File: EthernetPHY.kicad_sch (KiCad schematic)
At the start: 33 parts, among them IC2 DP83826IRHBR, J3 RJMG1S8008101BR, SW2 RESET, Y2 25MHz

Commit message: update
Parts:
- C11, C18: footprint Capacitor_SMD:C_0805_2012Metric -> Capacitor_SMD:C_0402_1005Metric; MPN (none) -> GRM155R71E103KA01D; Manufacturer (none) -> Murata Electronics
- C23: footprint Capacitor_SMD:C_0805_2012Metric -> Capacitor_SMD:C_0603_1608Metric
- D3, D4: footprint (none) -> LED_SMD:LED_0805_2012Metric
- SW2: value RESET -> SW_Push
- renumbered IC2 to U7
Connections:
- net +3.3V: now also C18.1; no longer C18.2
- net GND: now also C11.2, C18.2; no longer C11.1, C18.1
- net at C12.1, C13.1, C17.1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: now also C11.1; no longer C11.2
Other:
- note added: "PHY_RST"

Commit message: Done ERC + Documentation
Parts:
- added R36, R37, R42: 10k, Resistor_SMD:R_0603_1608Metric, symbol Device:R_US
- D8: renamed from D5; footprint ESD8104MUTAG -> footprints:ESD8104MUTAG; MPN (none) -> ESD7104MUTAG; Manufacturer_Part_Number ESD7104MUTAG -> (none)
- J6: renamed from J3; footprint RJMG1S8008101BR:AMPHENOL_RJMG1S8008101BR -> footprints:AMPHENOL_RJMG1S8008101BR; MPN (none) -> RJMG1S8008101BR
- renumbered C23 to C31, C22 to C32, C11 to C33, C12 to C34, C13 to C35, C15 to C36, C16 to C37, C14 to C38, C17 to C39, C18 to C40, C19 to C41, C20 to C42, C21 to C43, D4 to D10, D3 to D9, FB1 to FB2, R22 to R28, R16 to R29, R11 to R30, R13 to R31, R12 to R32, R14 to R33, R15 to R34, R18 to R35, R19 to R38, R23 to R39, R20 to R40, R21 to R41, SW2 to SW6, U7 to U5
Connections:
- net GND: now also R36.2, R37.2, R42.2
- net LED0: now also U5.30 (LED0/STRAP2)
- net at U5.22 (TX_CLK/STRAP5): now also R42.1
- net at U5.28 (COL/LED2/GPIO/STRAP4): now also R36.1
- net at U5.29 (CRS/LED3/STRAP3): now also R37.1
- no-connect marks 12 -> 9
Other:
- note added: "PHY Bootstrap table"
- moved on the sheet: C31, C32, C33, C34, C35, C36, C37, C38, C39, C40, C41, C42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

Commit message: Initial Review Changes
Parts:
- added TP5: RMII_REF_CLK, TestPoint:TestPoint_Pad_D1.0mm, symbol Connector:TestPoint
- J6: value RJMG1S8008101BR -> Ethernet
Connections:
- net REF_CLK: now also TP5.1
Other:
- company: (none) -> _electronic_projects
- title: (none) -> DeskNode-F4
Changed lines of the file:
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@@
 	(generator_version "9.0")
 	(paper "A4")
+	(title_block
+		(title "DeskNode-F4")
+		(rev "A")
+		(company "_electronic_projects")
+		(comment 1 "Wajahatulla Sharif")
+		(comment 2 "Designed by ")
+	)
 	(rectangle
 		(start 17.78 97.536)
@@
 	)
 	(junction
+		(at 231.14 93.98)
+		(diameter 0)
+		(color 0 0 0 0)
+	)
+	(junction
 		(at 30.48 142.24)
 		(diameter 0)
@@
 	(wire
 		(pts
+			(xy 231.14 64.77) (xy 231.14 93.98)
+		)
+		(stroke
+			(width 0)
+			(type default)
+		)
+	)
+	(wire
+		(pts
 			(xy 229.87 88.9) (xy 233.68 88.9)
 		)
@@
 	(wire
 		(pts
+			(xy 231.14 93.98) (xy 229.87 93.98)
+		)
+		(stroke
+			(width 0)
+			(type default)
+		)
+	)
+	(wire
+		(pts
 			(xy 40.64 81.28) (xy 40.64 85.09)
 		)
@@
 	(wire
 		(pts
-			(xy 237.49 93.98) (xy 229.87 93.98)
+			(xy 237.49 93.98) (xy 231.14 93.98)
 		)
 		(stroke
@@
 	)
 	(symbol
+		(lib_id "Connector:TestPoint")
+		(at 231.14 64.77 0)
+		(unit 1)
+		(exclude_from_sim no)
+		(in_bom yes)
+		(on_board yes)
+		(dnp no)
+		(fields_autoplaced yes)
+		(property "Reference" "TP5"
+			(at 233.68 60.1979 0)
+			(effects
+				(font
+					(size 1.27 1.27)
+				)
+				(justify left)
+			)
+		)
+		(property "Value" "RMII_REF_CLK"
+			(at 233.68 62.7379 0)
+			(effects
+				(font
+					(size 1.27 1.27)
+				)
+				(justify left)
+			)
+		)
+		(property "Footprint" "TestPoint:TestPoint_Pad_D1.0mm"
+			(at 236.22 64.77 0)
+			(effects
+				(font
+					(size 1.27 1.27)
+				)
+				(hide yes)
+			)
+		)
+		(property "Datasheet" "~"
+			(at 236.22 64.77 0)
+			(effects
+				(font
+					(size 1.27 1.27)
+				)
+				(hide yes)
+			)
+		)
+		(property "Description" "test point"
+			(at 231.14 64.77 0)
+			(effects
+				(font
+					(size 1.27 1.27)
+				)
+				(hide yes)
+			)
+		)
+		(pin "1"
+		)
+		(instances
+			(project "STM32 Microcontroller Board"
+				(path "/c703575f-b97a-4282-ae81-d5777b8a5a01/436b04a7-c6fa-4a3e-b66a-f6ad9cc4ab45"
+					(reference "TP5")
+					(unit 1)
+				)
+			)
+		)
+	)
+	(symbol
 		(lib_id "DP83826IRHBR:DP83826IRHBR")
 		(at 167.64 81.28 0)
@@
 			)
 		)
-		(property "Value" "RJMG1S8008101BR"
+		(property "Value" "Ethernet"
 			(at 39.37 26.67 0)
 			(effects

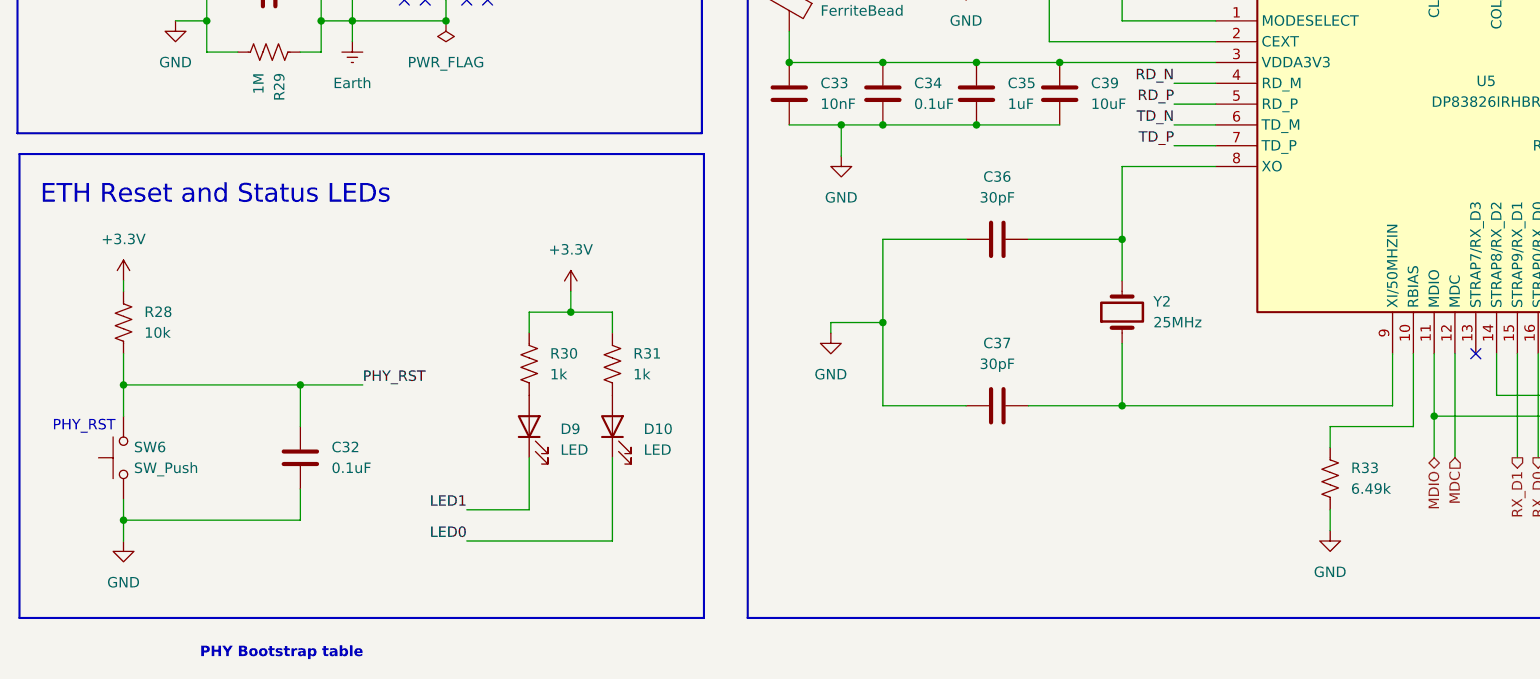
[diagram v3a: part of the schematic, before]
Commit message: MPNs updated
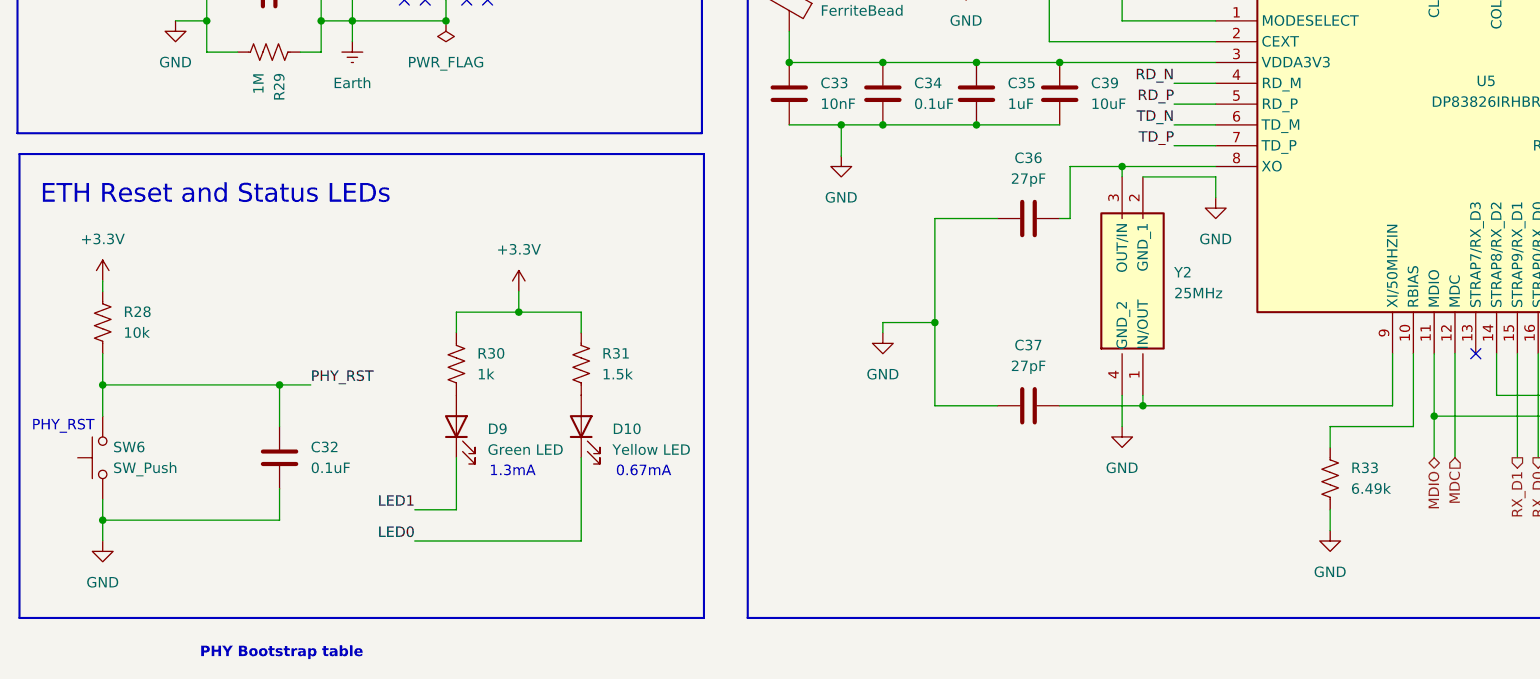
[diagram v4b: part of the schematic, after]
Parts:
- removed Y2: 25MHz, Crystal:Crystal_HC49-4H_Vertical, symbol Device:Crystal
- added Y2: 25MHz, footprints:ECS2501836B2CTYTR, symbol ECS-250-18-36B2-CTY-TR:ECS-250-18-36B2-CTY-TR
- C31: MPN (none) -> GRM188R72A102KA01D
- C36, C37: value 30pF -> 27pF; footprint Capacitor_SMD:C_0805_2012Metric -> Capacitor_SMD:C_0603_1608Metric; MPN (none) -> CL10C270JB8NNNC
- C38: footprint Capacitor_SMD:C_0402_1005Metric -> Capacitor_SMD:C_0603_1608Metric; MPN (none) -> GRM1885C1H202JA01D
- C39, C43: MPN (none) -> GRM21BR71A106KA73L; Manufacturer_Part_Number (none) -> GRM21BR71A106KA73L
- D10: value LED -> Yellow LED; MPN (none) -> APT2012SYCK
- D9: value LED -> Green LED; MPN (none) -> APT2012CGCK
- R28, R32, R34, R36, R37, R39, R40, R42: MPN (none) -> RC0603FR-0710KL
- R29: footprint Resistor_SMD:R_1206_3216Metric -> Resistor_SMD:R_0603_1608Metric; MPN (none) -> RC0603FR-071ML
- R30: MPN (none) -> RC0603FR-071KL
- R31: value 1k -> 1.5k; MPN (none) -> RC0603FR-071K5L
- R33: MPN (none) -> RC0603FR-076K49L
- R35, R38, R41: MPN (none) -> RC0603FR-072K49L
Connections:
- net +3.3V: now also R31.2; no longer R31.1
- net GND: now also Y2.2 (GND_1), Y2.4 (GND_2)
- net at D10.2 (A): now also R31.1; no longer R31.2
- net at C36.2, U5.8 (XO): now also Y2.3 (OUT/IN)
- net at C37.2, U5.9 (XI/50MHZIN): now also Y2.1 (IN/OUT)
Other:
- note added: "0.67mA"
- note added: "1.3mA"
- moved on the sheet: C32, R28, R30, SW6

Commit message: Layout placement
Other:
- note added: "ECS-250-18-36B2-CTY-TR"
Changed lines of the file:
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@@
 		)
 	)
+	(text "ECS-250-18-36B2-CTY-TR"
+		(exclude_from_sim no)
+		(at 148.336 114.046 90)
+		(effects
+			(font
+				(size 0.889 0.889)
+				(color 72 0 0 1)
+			)
+		)
+	)
 	(text "PHY Bootstrap table"
 		(exclude_from_sim no)
@@
 		(on_board yes)
 		(dnp no)
-		(fields_autoplaced yes)
 		(property "Reference" "J6"
-			(at 39.37 24.13 0)
+			(at 39.37 21.844 0)
 			(effects
 				(font
@@
 		)
 		(property "Value" "Ethernet"
-			(at 39.37 26.67 0)
+			(at 39.37 24.384 0)
 			(effects
 				(font
@@
 		)
 		(property "MPN" "RJMG1S8008101BR"
-			(at 39.37 44.45 0)
+			(at 39.624 26.924 0)
 			(effects
 				(font
 					(size 1.27 1.27)
 				)
-				(hide yes)
 			)
 		)
@@
 		(on_board yes)
 		(dnp no)
-		(fields_autoplaced yes)
 		(property "Reference" "Y2"
 			(at 158.75 112.0139 90)
@@
 				)
 				(justify left top)
-				(hide yes)
 			)
 		)
@@
 		(on_board yes)
 		(dnp no)
-		(fields_autoplaced yes)
 		(property "Reference" "FB2"
 			(at 115.57 77.5207 0)
@@
 		)
 		(property "MPN" "MPZ1608S601ATA00"
-			(at 111.76 78.74 0)
+			(at 120.65 82.296 0)
 			(effects
 				(font
-					(size 1.27 1.27)
+					(size 0.889 0.889)
 				)
-				(hide yes)
 			)
 		)

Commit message: Layout Routing
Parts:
- FB2: MPN MPZ1608S601ATA00 -> MPZ1608S601
- J6: MPN RJMG1S8008101BR -> RJMG1S8008101
- Y2: symbol ECS-250-18-36B2-CTY-TR:ECS-250-18-36B2-CTY-TR -> Device:Crystal_GND24
- renumbered C31 to C32, C32 to C33, C33 to C34, C34 to C35, C35 to C36, C38 to C37, C36 to C38, C37 to C39, C39 to C40, C40 to C41, C41 to C42, C42 to C43, C43 to C44, D8 to D10, D10 to D11
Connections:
- net RD_N: now also D10.5 (IO_4); no longer D10.1 (IO_1)
- net RD_P: now also D10.4 (IO_3); no longer D10.2 (IO_2)
- net TD_N: now also D10.2 (IO_2); no longer D10.4 (IO_3)
- net TD_P: now also D10.1 (IO_1); no longer D10.5 (IO_4)
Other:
- note added: "ECS2501836B2CTY"
- note removed: "ECS-250-18-36B2-CTY-TR"

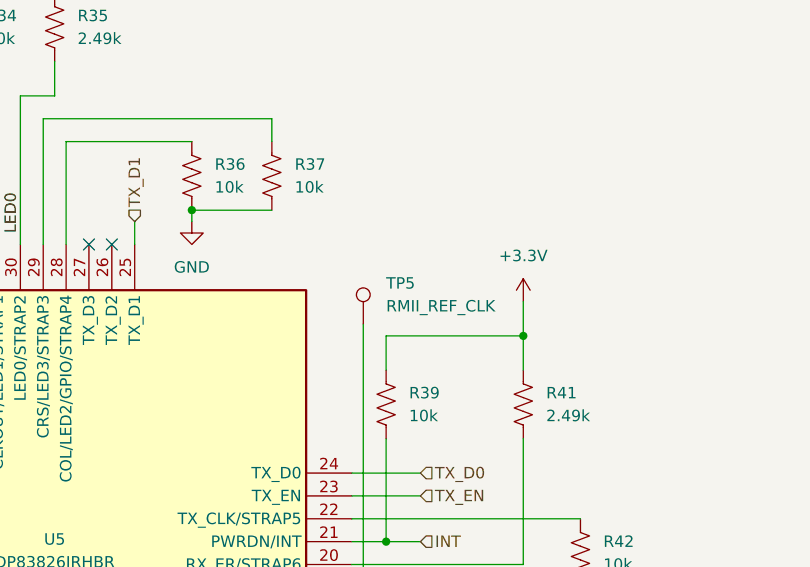
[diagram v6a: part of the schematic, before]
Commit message: Layout - 12V Power path
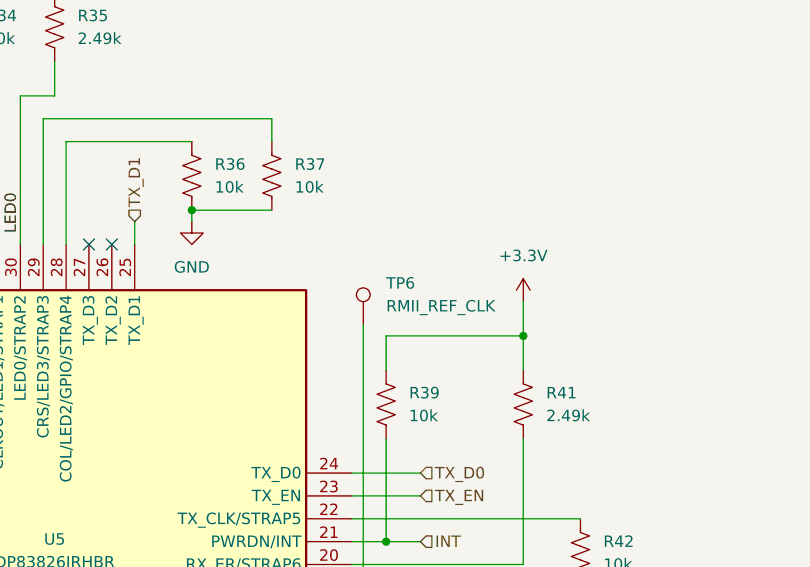
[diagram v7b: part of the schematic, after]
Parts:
- renumbered TP5 to TP6
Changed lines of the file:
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@@
 		(dnp no)
 		(fields_autoplaced yes)
-		(property "Reference" "TP5"
+		(property "Reference" "TP6"
 			(at 233.68 60.1979 0)
 			(effects
@@
 			(project "STM32 Microcontroller Board"
 				(path "/c703575f-b97a-4282-ae81-d5777b8a5a01/436b04a7-c6fa-4a3e-b66a-f6ad9cc4ab45"
-					(reference "TP5")
+					(reference "TP6")
 					(unit 1)
 				)

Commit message: Review files
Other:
- company: _electronic_projects -> (none)
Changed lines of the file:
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@@
 		(title "DeskNode-F4")
 		(rev "A")
-		(company "_electronic_projects")
-		(comment 1 "Wajahatulla Sharif")
-		(comment 2 "Designed by ")
 	)
 	(rectangle
